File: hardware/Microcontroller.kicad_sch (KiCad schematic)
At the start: 22 parts

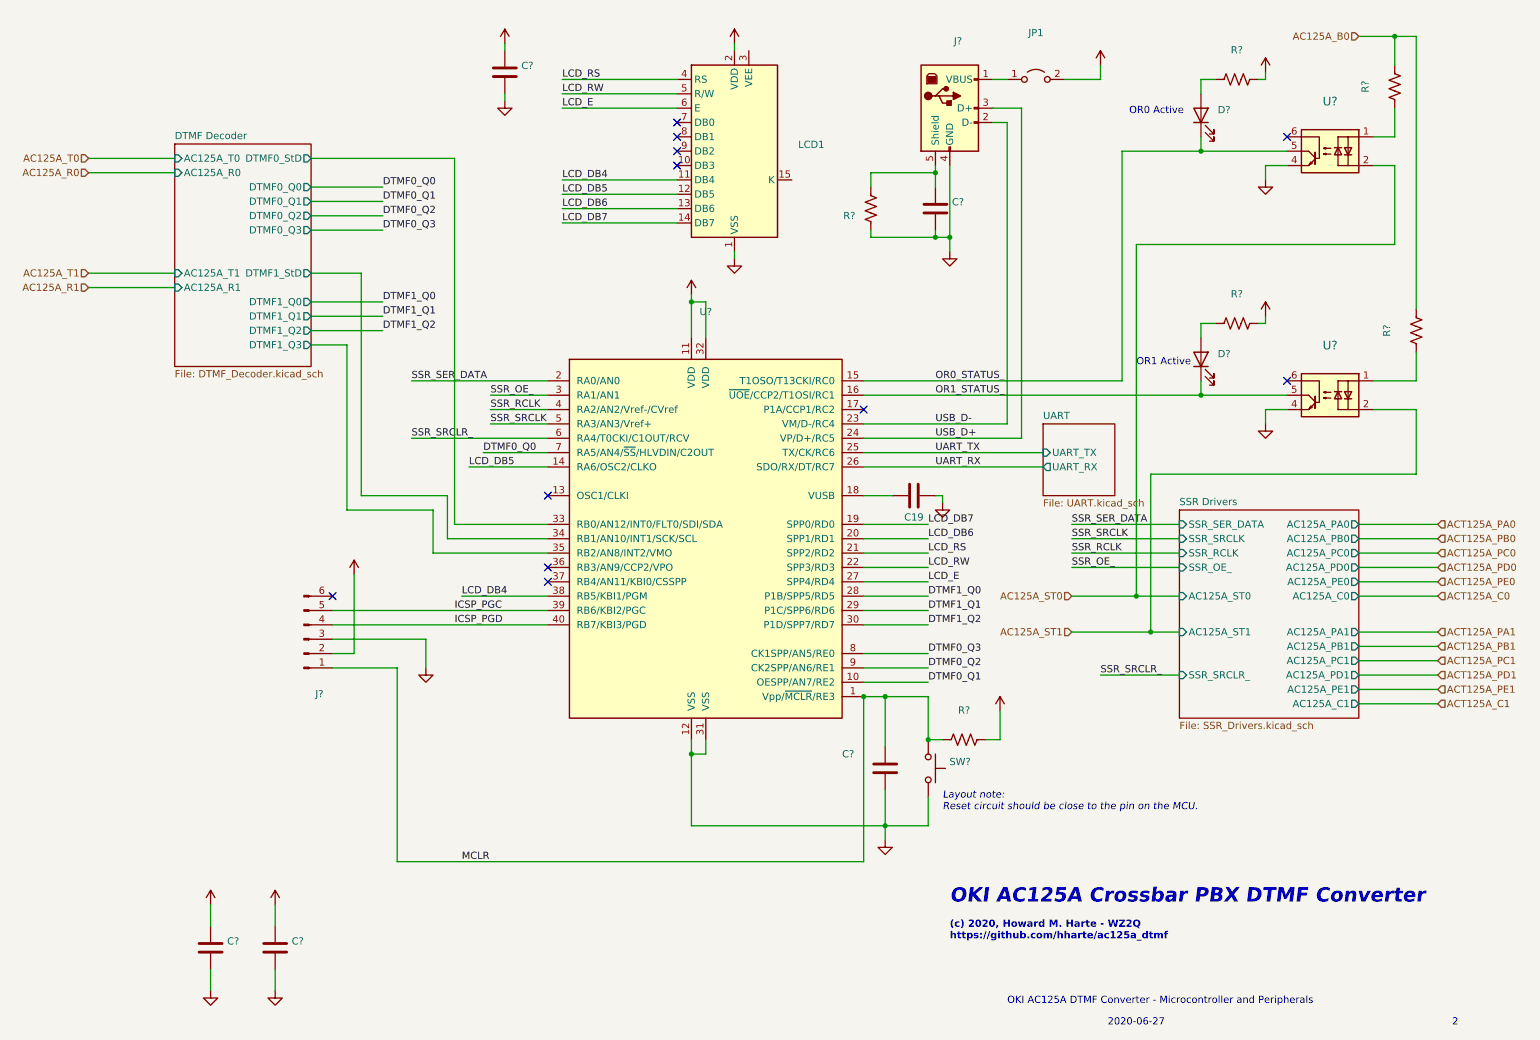
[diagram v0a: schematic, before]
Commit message: Fix a couple DRC errors in the layout.
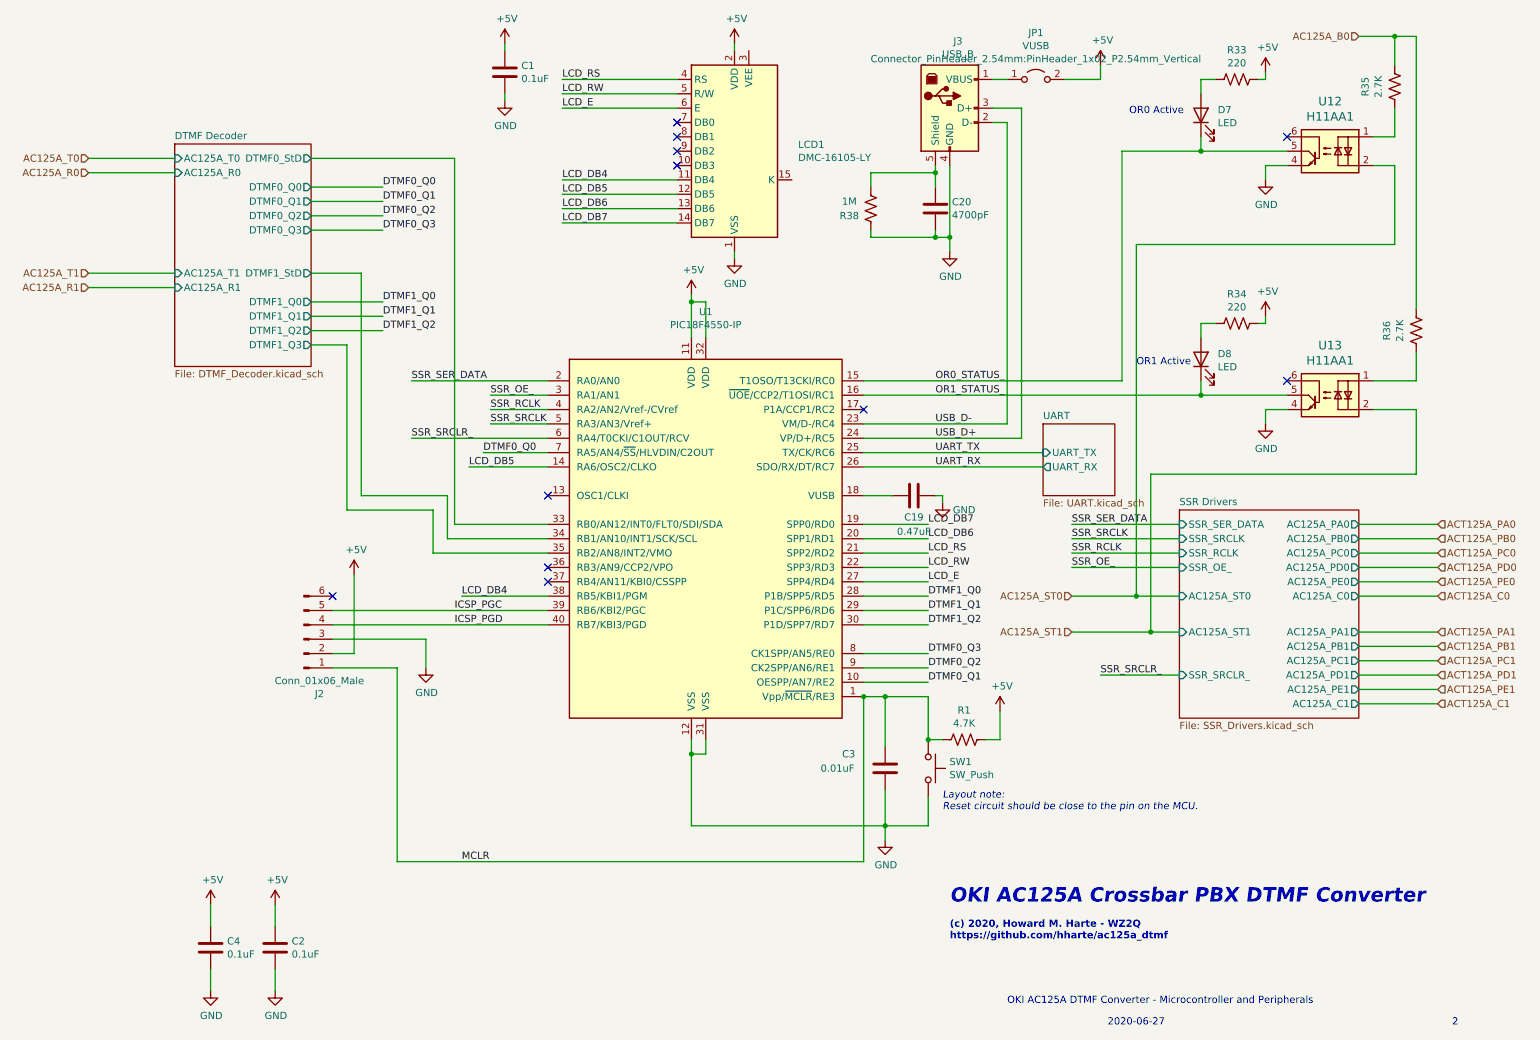
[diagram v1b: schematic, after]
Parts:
- C1, C2, C4: renamed from C?; value (none) -> 0.1uF; footprint (none) -> Capacitor_THT:C_Disc_D3.0mm_W2.0mm_P2.50mm
- C19: value (none) -> 0.47uF; footprint (none) -> Capacitor_THT:C_Disc_D3.0mm_W1.6mm_P2.50mm
- C20: renamed from C?; value (none) -> 4700pF; footprint (none) -> Capacitor_THT:C_Disc_D4.3mm_W1.9mm_P5.00mm
- C3: renamed from C?; value (none) -> 0.01uF; footprint (none) -> Capacitor_THT:C_Disc_D3.0mm_W1.6mm_P2.50mm
- D7, D8: renamed from D?; value (none) -> LED; footprint (none) -> LED_THT:LED_D5.0mm
- J2: renamed from J?; value (none) -> Conn_01x06_Male; footprint (none) -> Connector_PinHeader_2.54mm:PinHeader_1x06_P2.54mm_Vertical
- J3: renamed from J?; value (none) -> USB_B; footprint (none) -> Connector_USB:USB_B_OST_USB-B1HSxx_Horizontal
- JP1: value (none) -> VUSB; footprint (none) -> Connector_PinHeader_2.54mm:PinHeader_1x02_P2.54mm_Vertical
- LCD1: value (none) -> DMC-16105-LY; footprint (none) -> Connector_PinHeader_2.54mm:PinHeader_1x15_P2.54mm_Vertical
- R1: renamed from R?; value (none) -> 4.7K; footprint (none) -> Resistor_THT:R_Axial_DIN0207_L6.3mm_D2.5mm_P7.62mm_Horizontal
- R33, R34: renamed from R?; value (none) -> 220; footprint (none) -> Resistor_THT:R_Axial_DIN0207_L6.3mm_D2.5mm_P7.62mm_Horizontal
- R35, R36: renamed from R?; value (none) -> 2.7K; footprint (none) -> Resistor_THT:R_Axial_DIN0207_L6.3mm_D2.5mm_P7.62mm_Horizontal
- R38: renamed from R?; value (none) -> 1M; footprint (none) -> Resistor_THT:R_Axial_DIN0207_L6.3mm_D2.5mm_P7.62mm_Horizontal
- SW1: renamed from SW?; value (none) -> SW_Push; footprint (none) -> Button_Switch_THT:SW_PUSH_6mm
- U1: renamed from U?; value (none) -> PIC18F4550-IP; footprint (none) -> Package_DIP:DIP-40_W15.24mm
- U12, U13: renamed from U?; value (none) -> H11AA1; footprint (none) -> Package_DIP:DIP-6_W7.62mm

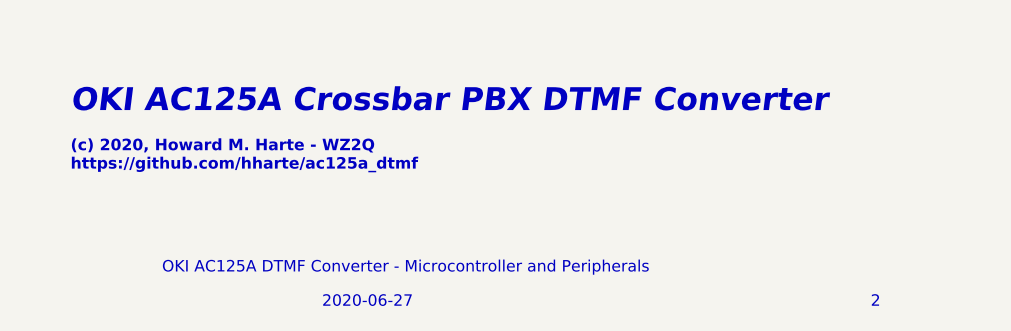
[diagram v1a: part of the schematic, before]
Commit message: Issue 3: Utilize we755a_dtmf boards.
     * Carrier for 2*we755a_dtmf boards.
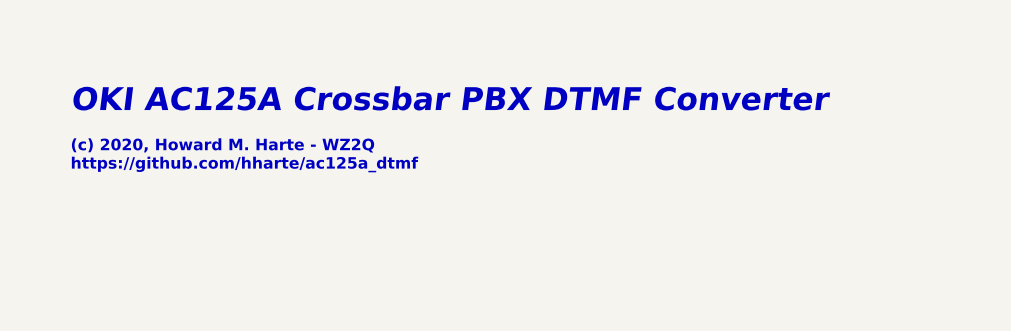
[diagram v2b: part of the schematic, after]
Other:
- note removed: "2"
- note removed: "2020-06-27"
- note removed: "OKI AC125A DTMF Converter - Microcontroller and Peripherals"
- title: (none) -> OKI AC125A DTMF Converter - Microcontroller and Peripherals
